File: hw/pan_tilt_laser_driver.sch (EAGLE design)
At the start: 37 parts, among them IC2 998-MIC5219-3.0YMM, IC3 FT2232H, IC5 93C46, IC6 998-MIC5219-3.0YMM, X1 798-ZX62RD-AB-5P8, X2 12MHz

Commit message: Outline replaced, in progress
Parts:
- removed C10, C11: 27pF, dp_devices:CAPC805
- removed C13: 4.7uF, dp_devices:CAP_POLSMC_A
- removed C14, C15, C16, C17, C18, C19, C20, C21, C22, C9: 0.1uF, dp_devices:CAPC805
- removed IC2, IC6: 998-MIC5219-3.0YMM, v-reg-micrel:MIC5219BMM
- removed IC3: FT2232H, DP-EagleLibrary:FT2232H
- removed R7: 10k, dp_devices:RESISTORR805R805
- removed X2: 12MHz, dp_devices:CRYSTAL_212M_
- added C1, C2, C31, C32: 0.1u, rcl:C-EUC0603K
- added C111, C56: C1608X5R1C106M080AB, SparkFun-Passives:CAP0603-CAP
- added C123: VJ0603A471KXQPW1BC, SparkFun-Passives:CAP0603-CAP
- added C28, C5: (no value), rcl:C-EUC0603K
- added C29, C30: 4.7u, rcl:C-EUC0603K
- added C90, C99: 18p, rcl:C-EUC0603K
- added J1: POWER_JACKPTH, SparkFun-Connectors:POWER_JACKPTH
- added R1: 10k, rcl:R-US_R0603
- added U1: CAT6219-330TDGT3, SparkFun-PowerIC:V_REG_MIC52195V
- added U2: (no value), torpedo:FT2232H
- added U3: LD3985M30R, SparkFun-PowerIC:V_REG_MIC52195V
- added Y1: 405I35D12M00000, SparkFun-FreqCtrl:CRYSTAL5X3
- C12: value 4.7uF -> 3.3u; device dp_devices:CAP_POLSMC_A -> rcl:C-EUC0603K
- C3: value C1608X5R1C106M080AB -> 0.1; device SparkFun-Passives:CAP0603-CAP -> rcl:C-EUC0603K
- C4: value C1608X5R1C106M080AB -> (none); device SparkFun-Passives:CAP0603-CAP -> rcl:C-EUC0603K
- C6: value VJ0603A471KXQPW1BC -> (none); device SparkFun-Passives:CAP0603-CAP -> rcl:C-EUC0603K
- C8: value 3.3uF -> .1u; device dp_devices:CAP_POLSMC_A -> rcl:C-EUC0603K
- JP2: value 651-5442251 -> (none); device SparkFun-Connectors:M03SCREW -> torpedo:M0322-03-5035
- L1, L2: value (none) -> BLM21PG331SN1D
- R2, R3, R4, R5, R6: device dp_devices:RESISTORR805R805 -> rcl:R-US_R0603
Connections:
- removed net !SUSPEND: IC3.SUSPEND#
- removed net +3V3: C24.1, IC6.OUT
- removed net N$2: C6.1, IC2.ADJ
- removed net PAN_TILT_RXD: IC3.BDBUS1/RXD/TDI/DO, JP2.1
- new net N$8: C25.1, U1.BP
- new net SERVO_POWER: J1.PWR, JP2.2
- net !RESET: now also R6.1, U2.RESET#; no longer IC3.RESET#, R3.2
- net 1.8V: now also C1.1, C12.1, C2.1, C3.1, U2.VCORE0, U2.VCORE1, U2.VCORE2, U2.VREGOUT; no longer C16.1, C17.1, C18.1, C8.+, IC3.VCORE0, IC3.VCORE1, IC3.VCORE2, IC3.VREGOUT
- net 3.3V: now also C24.1, C28.1, C4.1, C5.1, C6.1, C8.1, R1.2, R3.2, U1.OUT, U2.VCCIO0, U2.VCCIO1, U2.VCCIO2, U2.VCCIO3, U2.VREGIN; no longer C19.1, C20.1, C21.1, C22.1, C9.1, IC3.VCCIO0, IC3.VCCIO1, IC3.VCCIO2, IC3.VCCIO3, IC3.VREGIN, R3.1, R7.2
- net 5V: now also C56.1, U1.EN, U1.IN, U3.IN; no longer C3.1, IC2.IN, IC6.EN, IC6.IN
- net EECLK: now also R5.1, U2.EECLK; no longer IC3.EECLK, R7.1
- net EECS: now also R3.1, U2.EECS; no longer IC3.EECS, R6.1
- net EEDATA: now also R4.1, U2.EEDATA; no longer IC3.EEDATA, R4.2
- net GND: now also C1.2, C111.2, C12.2, C123.2, C2.2, C28.2, C29.2, C30.2, C31.2, C32.2, C5.2, C56.2, C8.2, C90.1, C99.1, J1.GND, J1.GNDBREAK, JP2.1, R2.2, U1.GND, U2.AGND, U2.GND0, U2.GND1, U2.GND2, U2.GND3, U2.GND4, U2.GND5, U2.GND6, U2.GND7, U2.TEST, U3.GND; no longer C10.1, C11.1, C12.-, C13.-, C14.2, C15.2, C16.2, C17.2, C18.2, C19.2, C20.2, C21.2, C22.2, C8.-, C9.2, IC2.GND, IC3.AGND, IC3.GND0, IC3.GND1, IC3.GND2, IC3.GND3, IC3.GND4, IC3.GND5, IC3.GND6, IC3.GND7, IC3.PWREN#, IC3.TEST, IC6.GND, JP2.3, R2.1
- net LASER_EN: now also U2.ADBUS4/DTR#/GPIOL0, U3.EN; no longer IC2.EN, IC3.ADBUS2/RTS#/TDO/DI
- net LASER_PWR: now also C111.1, U3.OUT; no longer C4.1, IC2.OUT
- net LASER_TXD: now also U2.ADBUS0/TXD/TCK/SK; no longer IC3.ADBUS0/TXD/TCK/SK
- net N$1: now also C123.1, U3.BP; no longer C25.1, IC6.ADJ
- net N$10: now also C90.2, U2.OSC0, Y1.1; no longer C11.2, IC3.OSC0, X2.X1
- net N$3: now also U2.DM; no longer IC3.DM
- net N$4: now also R2.1, U2.REF; no longer IC3.REF, R2.2
- net N$45: now also R1.1, R4.2; no longer R4.1, R5.1
- net N$5: now also U2.DP; no longer IC3.DP
- net N$6: now also C29.1, C31.1, U2.VPLL; no longer C12.+, C14.1, IC3.VPLL
- net N$7: now also C99.2, U2.OSCI, Y1.2; no longer C10.2, IC3.OSCI, X2.X2
- net N$9: now also C30.1, C32.1, U2.VPHY; no longer C13.+, C15.1, IC3.VPHY
- net PAN_TILT_TXD: now also JP2.3, U2.BDBUS0/TXD/TCK/SK; no longer IC3.BDBUS0/TXD/TCK/SK, JP2.2
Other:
- note removed: "5V->3V Regulator"
- note removed: "Laser Connector"
- note removed: "Laser: 3V @ 250mA"
- moved on the sheet: C23, C24, C25, C3, C4, C6, IC5, JP1, JP2, L2

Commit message: Preliminary placement complete.
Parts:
- removed C23, C56: C1608X5R1C106M080AB, SparkFun-Passives:CAP0603-CAP
- added C18: 3.3u, rcl:C-EUC0603K
- added C7: (no value), rcl:C-EUC0603K
- C12: value 3.3u -> .1u
- C4, C5: value (none) -> C1608X5R1C106M080AB; device rcl:C-EUC0603K -> SparkFun-Passives:CAP0603-CAP
- C8: value .1u -> (none)
- JP1: value 651-5442251 -> (none); device SparkFun-Connectors:M03SCREW -> torpedo:M0322-03-5035
- JP2: value (none) -> 651-5442251; device torpedo:M0322-03-5035 -> SparkFun-Connectors:M03SCREW
- R2: value 12k 1% -> 2.2k
- R4: value 2.2k -> 10k
- R5: value 10k -> 12k 1%
- U2: value (none) -> LD3985M30R; device torpedo:FT2232H -> SparkFun-PowerIC:V_REG_MIC52195V
- U3: value LD3985M30R -> (none); device SparkFun-PowerIC:V_REG_MIC52195V -> torpedo:FT2232H
- renumbered C111 to C14, C123 to C11, C24 to C13, C25 to C10, C28 to C9, C29 to C17, C30 to C19, C31 to C20, C32 to C21, C90 to C16, C99 to C15, IC5 to IC1
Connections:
- net !RESET: now also U3.RESET#; no longer U2.RESET#
- net 1.8V: now also C18.1, U3.VCORE0, U3.VCORE1, U3.VCORE2, U3.VREGOUT; no longer C12.1, U2.VCORE0, U2.VCORE1, U2.VCORE2, U2.VREGOUT
- net 3.3V: now also C12.1, C7.1, R4.2, U3.VCCIO0, U3.VCCIO1, U3.VCCIO2, U3.VCCIO3, U3.VREGIN; no longer C4.1, C5.1, R5.2, U2.VCCIO0, U2.VCCIO1, U2.VCCIO2, U2.VCCIO3, U2.VREGIN
- net 5V: now also C4.1, C5.1, U2.IN; no longer C23.1, C56.1, U3.IN
- net EECLK: now also R4.1, U3.EECLK; no longer R5.1, U2.EECLK
- net EECS: now also U3.EECS; no longer U2.EECS
- net EEDATA: now also R2.1, U3.EEDATA; no longer R4.1, U2.EEDATA
- net GND: now also C18.2, C7.2, JP1.1, JP2.3, R5.2, U2.GND, U3.AGND, U3.GND0, U3.GND1, U3.GND2, U3.GND3, U3.GND4, U3.GND5, U3.GND6, U3.GND7, U3.TEST; no longer C23.2, C56.2, JP1.3, JP2.1, R2.2, U2.AGND, U2.GND0, U2.GND1, U2.GND2, U2.GND3, U2.GND4, U2.GND5, U2.GND6, U2.GND7, U2.TEST, U3.GND
- net LASER_EN: now also U2.EN, U3.ADBUS4/DTR#/GPIOL0; no longer U2.ADBUS4/DTR#/GPIOL0, U3.EN
- net LASER_PWR: now also JP2.1, U2.OUT; no longer JP1.1, U3.OUT
- net LASER_TXD: now also JP2.2, U3.ADBUS0/TXD/TCK/SK; no longer JP1.2, U2.ADBUS0/TXD/TCK/SK
- net N$1: now also U2.BP; no longer U3.BP
- net N$10: now also U3.OSC0; no longer U2.OSC0
- net N$3: now also U3.DM; no longer U2.DM
- net N$4: now also R5.1, U3.REF; no longer R2.1, U2.REF
- net N$45: now also R2.2; no longer R4.2
- net N$5: now also U3.DP; no longer U2.DP
- net N$6: now also U3.VPLL; no longer U2.VPLL
- net N$7: now also U3.OSCI; no longer U2.OSCI
- net N$9: now also U3.VPHY; no longer U2.VPHY
- net PAN_TILT_TXD: now also JP1.3, U3.BDBUS0/TXD/TCK/SK; no longer JP2.3, U2.BDBUS0/TXD/TCK/SK
- net SERVO_POWER: now also JP1.2; no longer JP2.2
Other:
- moved on the sheet: C12, C4, C5, C6, C8, JP1, JP2, R2, R4, R5

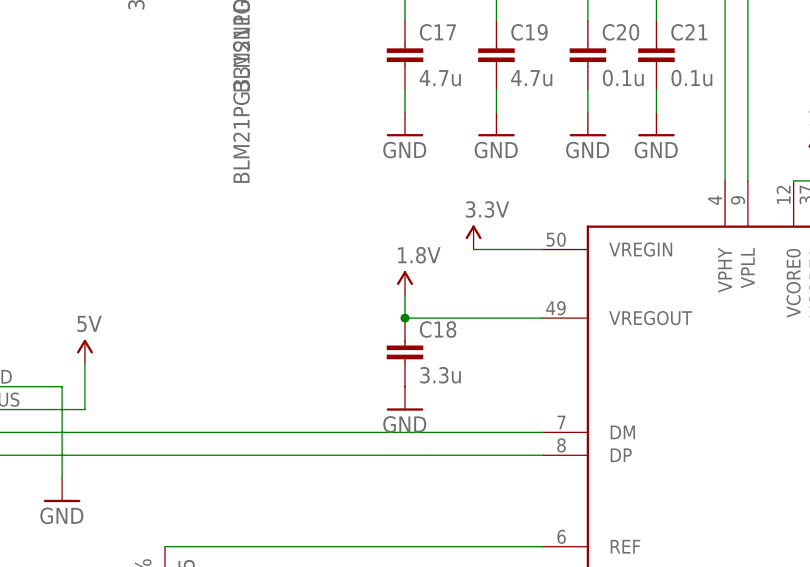
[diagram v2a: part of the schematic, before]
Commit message: Finished initial routing.
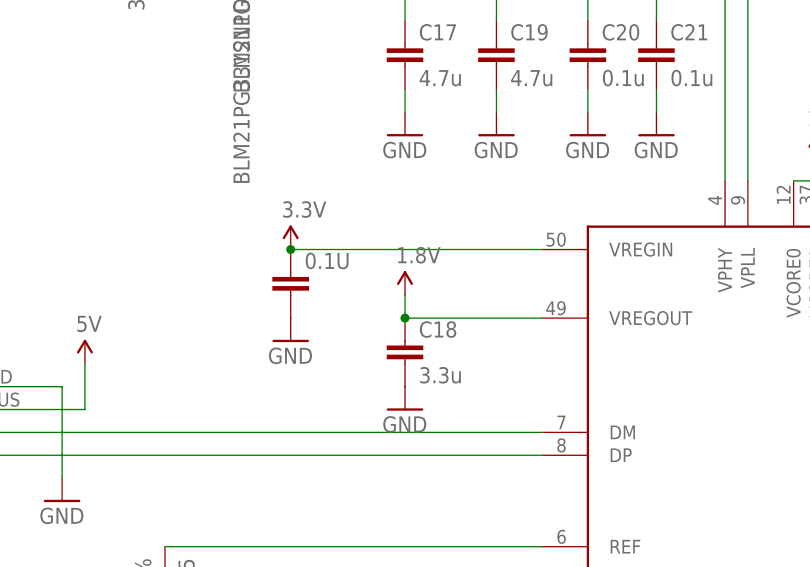
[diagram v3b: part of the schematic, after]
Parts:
- added 0.1U: (no value), rcl:C-EUC0603K
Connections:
- net 3.3V: now also 0.1U.1
- net GND: now also 0.1U.2
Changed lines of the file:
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@@
 <setting verticaltext="up"/>
 </settings>
-<grid distance="0.1" unitdist="inch" unit="inch" style="lines" multiple="1" display="yes" altdistance="0.01" altunitdist="inch" altunit="inch"/>
+<grid distance="0.1" unitdist="inch" unit="inch" style="lines" multiple="1" display="no" altdistance="0.01" altunitdist="inch" altunit="inch"/>
 <layers>
 <layer number="1" name="Top" color="4" fill="1" visible="no" active="no"/>
@@
 <part name="SUPPLY2" library="SparkFun-Aesthetics" deviceset="5V" device=""/>
 <part name="SUPPLY3" library="SparkFun-Aesthetics" deviceset="5V" device=""/>
+<part name="0.1U" library="rcl" deviceset="C-EU" device="C0603K"/>
+<part name="GND24" library="supply1" deviceset="GND" device=""/>
 </parts>
 <sheets>
@@
 <attribute name="VALUE" x="92.71" y="220.98" size="1.778" layer="96" rot="R270"/>
 </instance>
-<instance part="P+8" gate="G$1" x="119.38" y="182.88"/>
+<instance part="P+8" gate="G$1" x="99.06" y="182.88"/>
 <instance part="GND18" gate="1" x="111.76" y="165.1"/>
 <instance part="GND12" gate="1" x="85.09" y="137.16"/>
@@
 <instance part="SUPPLY2" gate="G$1" x="30.48" y="48.26"/>
 <instance part="SUPPLY3" gate="G$1" x="30.48" y="2.54"/>
+<instance part="0.1U" gate="G$1" x="99.06" y="180.34"/>
+<instance part="GND24" gate="1" x="99.06" y="172.72"/>
 </instances>
 <busses>
@@
 <junction x="170.18" y="78.74"/>
 </segment>
+<segment>
+<pinref part="0.1U" gate="G$1" pin="2"/>
+<pinref part="GND24" gate="1" pin="GND"/>
+</segment>
 </net>
 <net name="3.3V" class="1">
 <segment>
-<wire x1="127" y1="182.88" x2="119.38" y2="182.88" width="0.1524" layer="91"/>
+<wire x1="127" y1="182.88" x2="99.06" y2="182.88" width="0.1524" layer="91"/>
 <pinref part="P+8" gate="G$1" pin="3.3V"/>
 <pinref part="U3" gate="G$1" pin="VREGIN"/>
-</segment>
-<segment>
+<pinref part="0.1U" gate="G$1" pin="1"/>
+<junction x="99.06" y="182.88"/>
+</segment>
+<segment>

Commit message: Final version of the ref hw.
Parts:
- added LED1, LED2: (no value), SparkFun-LED:LED1206
- added R7, R8: 330, rcl:R-US_R0603
- C10, C11: value VJ0603A471KXQPW1BC -> 0.01u
- C12: value .1u -> 0.1u
- C13, C14, C4, C5: value C1608X5R1C106M080AB -> 10u
- C18: value 3.3u -> 10u
- C22, C6, C7, C8, C9: value (none) -> 0.1u
- C3: value 0.1 -> 0.1u
- renumbered 0.1U to C22
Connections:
- new net N$11: LED2.A, R8.2
- new net N$2: LED1.A, R7.2
- net 3.3V: now also R8.1
- net GND: now also LED1.C, LED2.C
- net SERVO_POWER: now also R7.1
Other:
- moved on the sheet: R5, R6
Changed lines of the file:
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@@
 <part name="GND20" library="supply1" deviceset="GND" device=""/>
 <part name="GND3" library="supply1" deviceset="GND" device=""/>
-<part name="C4" library="SparkFun-Passives" deviceset="CAP" device="0603-CAP" value="C1608X5R1C106M080AB"/>
-<part name="C13" library="SparkFun-Passives" deviceset="CAP" device="0603-CAP" value="C1608X5R1C106M080AB"/>
-<part name="C10" library="SparkFun-Passives" deviceset="CAP" device="0603-CAP" value="VJ0603A471KXQPW1BC"/>
+<part name="C4" library="SparkFun-Passives" deviceset="CAP" device="0603-CAP" value="10u"/>
+<part name="C13" library="SparkFun-Passives" deviceset="CAP" device="0603-CAP" value="10u"/>
+<part name="C10" library="SparkFun-Passives" deviceset="CAP" device="0603-CAP" value="0.01u"/>
 <part name="GND10" library="supply1" deviceset="GND" device=""/>
 <part name="GND23" library="supply1" deviceset="GND" device=""/>
@@
 <part name="C1" library="rcl" deviceset="C-EU" device="C0603K" value="0.1u"/>
 <part name="C2" library="rcl" deviceset="C-EU" device="C0603K" value="0.1u"/>
-<part name="C3" library="rcl" deviceset="C-EU" device="C0603K" value="0.1"/>
-<part name="C6" library="rcl" deviceset="C-EU" device="C0603K"/>
-<part name="C7" library="rcl" deviceset="C-EU" device="C0603K"/>
-<part name="C8" library="rcl" deviceset="C-EU" device="C0603K"/>
-<part name="C9" library="rcl" deviceset="C-EU" device="C0603K"/>
+<part name="C3" library="rcl" deviceset="C-EU" device="C0603K" value="0.1u"/>
+<part name="C6" library="rcl" deviceset="C-EU" device="C0603K" value="0.1u"/>
+<part name="C7" library="rcl" deviceset="C-EU" device="C0603K" value="0.1u"/>
+<part name="C8" library="rcl" deviceset="C-EU" device="C0603K" value="0.1u"/>
+<part name="C9" library="rcl" deviceset="C-EU" device="C0603K" value="0.1u"/>
 <part name="C17" library="rcl" deviceset="C-EU" device="C0603K" value="4.7u"/>
 <part name="C19" library="rcl" deviceset="C-EU" device="C0603K" value="4.7u"/>
@@
 <part name="R6" library="rcl" deviceset="R-US_" device="R0603" value="10k"/>
 <part name="R5" library="rcl" deviceset="R-US_" device="R0603" value="12k 1%"/>
-<part name="C18" library="rcl" deviceset="C-EU" device="C0603K" value="3.3u"/>
-<part name="C12" library="rcl" deviceset="C-EU" device="C0603K" value=".1u"/>
+<part name="C18" library="rcl" deviceset="C-EU" device="C0603K" value="10u"/>
+<part name="C12" library="rcl" deviceset="C-EU" device="C0603K" value="0.1u"/>
 <part name="C15" library="rcl" deviceset="C-EU" device="C0603K" value="18p"/>
 <part name="C16" library="rcl" deviceset="C-EU" device="C0603K" value="18p"/>
@@
 <part name="GND6" library="supply1" deviceset="GND" device=""/>
 <part name="GND4" library="supply1" deviceset="GND" device=""/>
-<part name="C5" library="SparkFun-Passives" deviceset="CAP" device="0603-CAP" value="C1608X5R1C106M080AB"/>
-<part name="C14" library="SparkFun-Passives" deviceset="CAP" device="0603-CAP" value="C1608X5R1C106M080AB"/>
-<part name="C11" library="SparkFun-Passives" deviceset="CAP" device="0603-CAP" value="VJ0603A471KXQPW1BC"/>
+<part name="C5" library="SparkFun-Passives" deviceset="CAP" device="0603-CAP" value="10u"/>
+<part name="C14" library="SparkFun-Passives" deviceset="CAP" device="0603-CAP" value="10u"/>
+<part name="C11" library="SparkFun-Passives" deviceset="CAP" device="0603-CAP" value="0.01u"/>
 <part name="GND11" library="supply1" deviceset="GND" device=""/>
 <part name="U2" library="SparkFun-PowerIC" deviceset="V_REG_MIC5219" device="5V" value="LD3985M30R"/>
@@
 <part name="SUPPLY2" library="SparkFun-Aesthetics" deviceset="5V" device=""/>
 <part name="SUPPLY3" library="SparkFun-Aesthetics" deviceset="5V" device=""/>
-<part name="0.1U" library="rcl" deviceset="C-EU" device="C0603K"/>
+<part name="C22" library="rcl" deviceset="C-EU" device="C0603K" value="0.1u"/>
 <part name="GND24" library="supply1" deviceset="GND" device=""/>
+<part name="R7" library="rcl" deviceset="R-US_" device="R0603" value="330"/>
+<part name="R8" library="rcl" deviceset="R-US_" device="R0603" value="330"/>
+<part name="LED1" library="SparkFun-LED" deviceset="LED" device="1206"/>
+<part name="LED2" library="SparkFun-LED" deviceset="LED" device="1206"/>
+<part name="GND25" library="supply1" deviceset="GND" device=""/>
+<part name="GND26" library="supply1" deviceset="GND" device=""/>
+<part name="P+10" library="SparkFun" deviceset="3.3V" device=""/>
 </parts>
 <sheets>
@@
 <instance part="L1" gate="G$1" x="99.06" y="223.52" smashed="yes" rot="R270">
 <attribute name="NAME" x="98.044" y="226.314" size="1.778" layer="95"/>
-<attribute name="VALUE" x="92.71" y="220.98" size="1.778" layer="96" rot="R270"/>
+<attribute name="VALUE" x="93.98" y="228.6" size="1.778" layer="96"/>
 </instance>
 <instance part="P+8" gate="G$1" x="99.06" y="182.88"/>
 <instance part="GND18" gate="1" x="111.76" y="165.1"/>
-<instance part="GND12" gate="1" x="85.09" y="137.16"/>
+<instance part="GND12" gate="1" x="83.82" y="137.16"/>
 <instance part="P+7" gate="G$1" x="96.52" y="142.24" rot="R90"/>
 <instance part="IC1" gate="G$1" x="63.5" y="111.76"/>
@@
 <instance part="L2" gate="G$1" x="99.06" y="213.36" smashed="yes" rot="R270">
 <attribute name="NAME" x="98.044" y="216.154" size="1.778" layer="95"/>
-<attribute name="VALUE" x="92.71" y="210.82" size="1.778" layer="96" rot="R270"/>
+<attribute name="VALUE" x="86.36" y="208.28" size="1.778" layer="96"/>
 </instance>
 <instance part="GND17" gate="1" x="111.76" y="195.58"/>
@@
 <instance part="R3" gate="G$1" x="50.8" y="137.16" rot="R90"/>
 <instance part="R4" gate="G$1" x="66.04" y="137.16" rot="R90"/>
-<instance part="R6" gate="G$1" x="107.95" y="142.24" rot="R180"/>
-<instance part="R5" gate="G$1" x="85.09" y="144.78" rot="R270"/>
+<instance part="R6" gate="G$1" x="109.22" y="142.24" rot="R180"/>
+<instance part="R5" gate="G$1" x="83.82" y="144.78" rot="R270"/>
 <instance part="C18" gate="G$1" x="111.76" y="172.72"/>
 <instance part="C12" gate="G$1" x="88.9" y="114.3"/>
@@
 <instance part="SUPPLY2" gate="G$1" x="30.48" y="48.26"/>
 <instance part="SUPPLY3" gate="G$1" x="30.48" y="2.54"/>
-<instance part="0.1U" gate="G$1" x="99.06" y="180.34"/>
+<instance part="C22" gate="G$1" x="99.06" y="180.34"/>
 <instance part="GND24" gate="1" x="99.06" y="172.72"/>
+<instance part="R7" gate="G$1" x="-88.9" y="106.68" rot="R270"/>
+<instance part="R8" gate="G$1" x="-71.12" y="106.68" rot="R270"/>
+<instance part="LED1" gate="G$1" x="-88.9" y="93.98"/>
+<instance part="LED2" gate="G$1" x="-71.12" y="93.98"/>
+<instance part="GND25" gate="1" x="-88.9" y="86.36"/>
+<instance part="GND26" gate="1" x="-71.12" y="86.36"/>
+<instance part="P+10" gate="G$1" x="-71.12" y="114.3"/>
 </instances>
 <busses>
@@
 </segment>
 <segment>
-<pinref part="0.1U" gate="G$1" pin="2"/>
+<pinref part="C22" gate="G$1" pin="2"/>
 <pinref part="GND24" gate="1" pin="GND"/>
+</segment>
+<segment>
+<pinref part="LED1" gate="G$1" pin="C"/>
+<pinref part="GND25" gate="1" pin="GND"/>
+</segment>
+<segment>
+<pinref part="LED2" gate="G$1" pin="C"/>
+<pinref part="GND26" gate="1" pin="GND"/>
 </segment>
 </net>
@@
 <pinref part="P+8" gate="G$1" pin="3.3V"/>
 <pinref part="U3" gate="G$1" pin="VREGIN"/>
-<pinref part="0.1U" gate="G$1" pin="1"/>
+<pinref part="C22" gate="G$1" pin="1"/>
 <junction x="99.06" y="182.88"/>
 </segment>
 <segment>
-<wire x1="96.52" y1="142.24" x2="102.87" y2="142.24" width="0.1524" layer="91"/>
+<wire x1="96.52" y1="142.24" x2="104.14" y2="142.24" width="0.1524" layer="91"/>
 <pinref part="P+7" gate="G$1" pin="3.3V"/>
 <pinref part="R6" gate="G$1" pin="2"/>
@@
 <junction x="99.06" y="43.18"/>
 </segment>
+<segment>
+<pinref part="R8" gate="G$1" pin="1"/>
+<pinref part="P+10" gate="G$1" pin="3.3V"/>
+<wire x1="-71.12" y1="114.3" x2="-71.12" y2="111.76" width="0.1524" layer="91"/>
+</segment>
 </net>
 <net name="LASER_TXD" class="0">
@@
 <net name="N$4" class="0">
 <segment>
-<wire x1="127" y1="149.86" x2="85.09" y2="149.86" width="0.1524" layer="91"/>
+<wire x1="127" y1="149.86" x2="83.82" y2="149.86" width="0.1524" layer="91"/>
 <pinref part="R5" gate="G$1" pin="1"/>
 <pinref part="U3" gate="G$1" pin="REF"/>
@@
 <net name="!RESET" class="0">
 <segment>
-<wire x1="127" y1="142.24" x2="113.03" y2="142.24" width="0.1524" layer="91"/>
+<wire x1="127" y1="142.24" x2="114.3" y2="142.24" width="0.1524" layer="91"/>
 <label x="115.57" y="142.24" size="1.778" layer="95"/>
 <pinref part="R6" gate="G$1" pin="1"/>
@@
 <pinref part="JP1" gate="G$1" pin="2"/>
 </segment>
+<segment>
+<pinref part="R7" gate="G$1" pin="1"/>
+<wire x1="-88.9" y1="111.76" x2="-109.22" y2="111.76" width="0.1524" layer="91"/>
+<label x="-106.68" y="111.76" size="1.778" layer="95"/>
+</segment>
 </net>
 <net name="N$8" class="0">
@@
 </segment>
 </net>
+<net name="N$2" class="0">
+<segment>
+<pinref part="R7" gate="G$1" pin="2"/>
+<pinref part="LED1" gate="G$1" pin="A"/>
+<wire x1="-88.9" y1="101.6" x2="-88.9" y2="96.52" width="0.1524" layer="91"/>
+</segment>
+</net>
+<net name="N$11" class="0">
+<segment>
+<pinref part="R8" gate="G$1" pin="2"/>
+<pinref part="LED2" gate="G$1" pin="A"/>
+<wire x1="-71.12" y1="101.6" x2="-71.12" y2="96.52" width="0.1524" layer="91"/>
+</segment>
+</net>

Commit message: Fix part number for USB micro connector (was wrong direction part -- upside down).
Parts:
- X1: value 798-ZX62RD-AB-5P8 -> 538-47346-0001
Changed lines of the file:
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@@
 </classes>
 <parts>
-<part name="X1" library="SparkFun" deviceset="USB" device="-MICROB" value="798-ZX62RD-AB-5P8"/>
+<part name="X1" library="SparkFun" deviceset="USB" device="-MICROB" value="538-47346-0001"/>
 <part name="GND8" library="SparkFun" deviceset="GND" device=""/>
 <part name="GND16" library="SparkFun" deviceset="GND" device=""/>
